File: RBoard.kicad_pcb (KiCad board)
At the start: 4 copper layers, 55 x 55 mm, 91 parts, among them J400 Conn_01x02, J401 SWD, J402 USB_B_Micro, J403 Conn_01x04, J404 Conn_01x04, J405 Conn_01x04, J406 Conn_01x04, J407 Conn_01x04, J408 Conn_01x04, Q100 AO3401A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

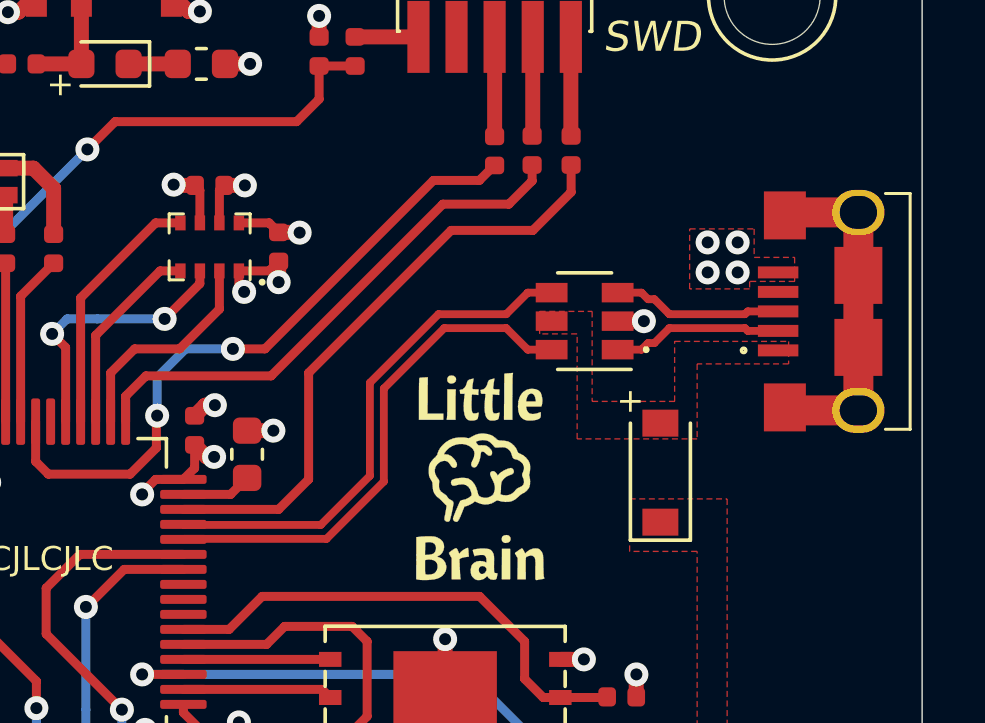
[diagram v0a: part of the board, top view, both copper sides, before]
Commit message: Changed USB connector.
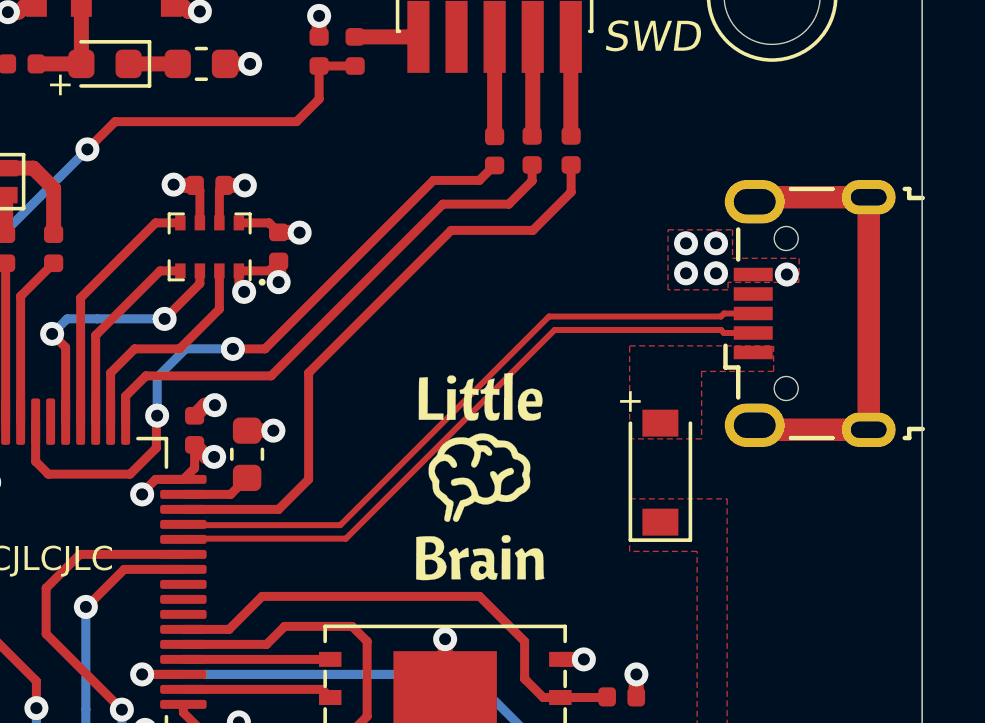
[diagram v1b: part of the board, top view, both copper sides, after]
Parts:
- removed U400: USBLC6-2SC6, Package_TO_SOT_SMD:SOT-23-6
- J402: footprint SchmillipKiCADLibrary:USB_MICRO_B_101181930001LF -> Connector_USB:USB_Micro-B_Wuerth_629105150521
- moved J402 1.53 mm to (178.8, 41.3)
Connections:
- J401 pad 7: Net-(J401-Pad7) -> (no net)
- J401 pad 8: Net-(J401-Pad8) -> (no net)
- J402 pad 2: USB_CONN_D- -> USB_D-
- J402 pad 3: USB_CONN_D+ -> USB_D+
- J402 pad 4: Net-(J402-Pad4) -> (no net)
- U200 pad 2: Net-(U200-Pad2) -> (no net)
- U200 pad 25: Net-(U200-Pad25) -> (no net)
- U200 pad 3: Net-(U200-Pad3) -> (no net)
- U200 pad 39: Net-(U200-Pad39) -> (no net)
- U200 pad 4: Net-(U200-Pad4) -> (no net)
- U200 pad 40: Net-(U200-Pad40) -> (no net)
- U200 pad 41: Net-(U200-Pad41) -> (no net)
- U200 pad 54: Net-(U200-Pad54) -> (no net)
- U200 pad 59: Net-(U200-Pad59) -> (no net)
- U200 pad 8: Net-(U200-Pad8) -> (no net)
- U200 pad 9: Net-(U200-Pad9) -> (no net)
- U301 pad 1: Net-(U301-Pad1) -> (no net)
- U301 pad 13: Net-(U301-Pad13) -> (no net)
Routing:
- net USB_CONN_D-: track 5.69 -> 0.00 mm
- net USB_CONN_D+: track 5.69 -> 0.00 mm
- net USB_D-: track 17.3 -> 22.0 mm
- net USB_D+: track 17.3 -> 22.0 mm
- net Net-(J402-Pad6): track 11.6 -> 15.5 mm
- net GND: track 59.9 -> 59.1 mm
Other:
- rule pad_to_mask_clearance: 0.05 -> 0
